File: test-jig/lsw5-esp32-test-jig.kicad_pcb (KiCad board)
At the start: 2 copper layers, 53.8 x 100 mm, 25 parts, among them J1 Conn_02x03_Odd_Even, J2 Conn_02x05_Odd_Even, J3 Conn_02x03_Odd_Even, J4 Conn_02x05_Odd_Even, J5 USB4105-GF-A, SW1 DUT, SW2 USB, U1 LD1117V33, U2 MCP2221AxSL

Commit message: test jig: Fix MCP2221A V_USB capacitor value
DS20005565E-page 17

> The VUSB pin requires an external bypass capacitor
> with a value between 0.22 and 0.47 μF (ceramic cap)
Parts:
- C4: value 1μ -> 470n
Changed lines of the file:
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@@
 			)
 		)
-		(property "Value" "1μ"
+		(property "Value" "470n"
 			(at 0 1.43 90)
 			(layer "F.Fab")

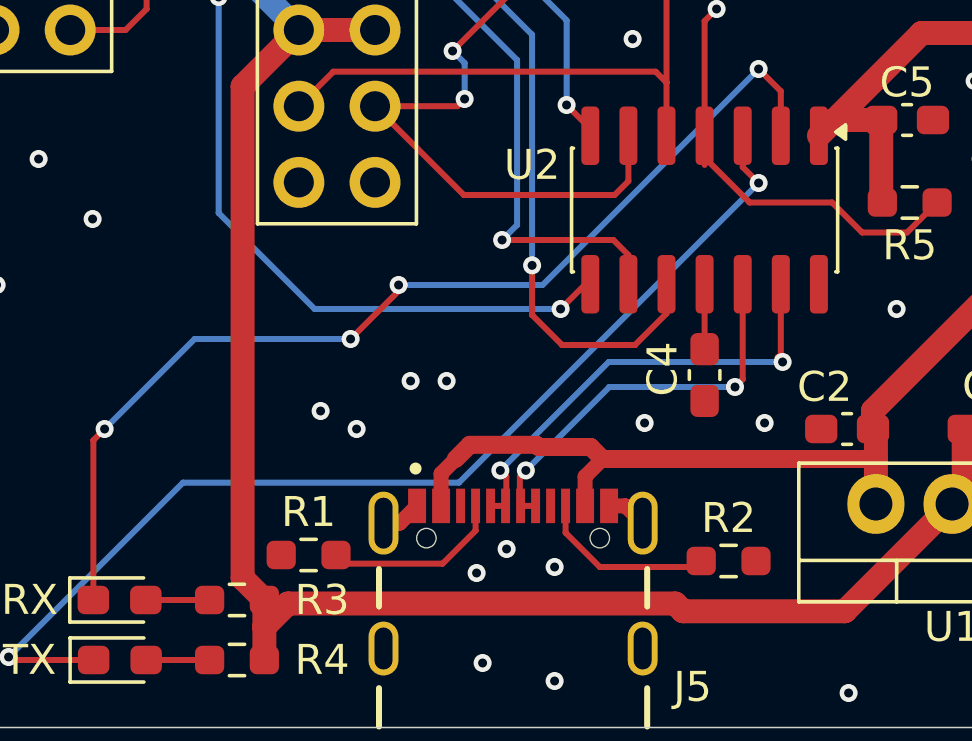
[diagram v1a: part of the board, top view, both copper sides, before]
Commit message: test jig: Fix USB only working on one side
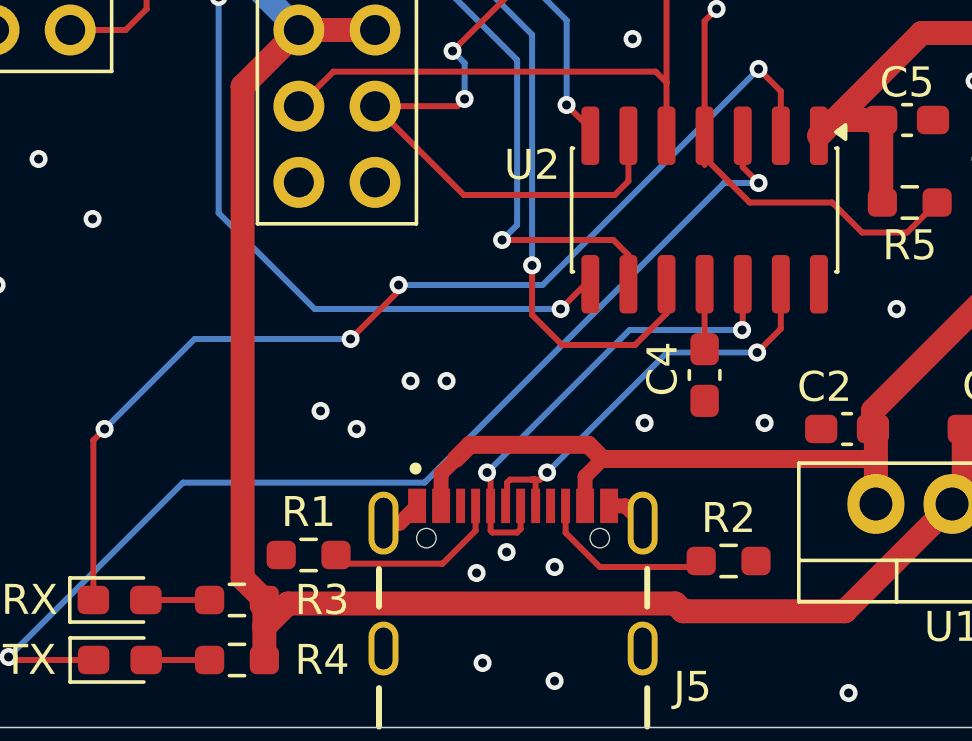
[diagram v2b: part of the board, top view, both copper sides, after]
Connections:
- J5 pad B6: /USB_DN -> /USB_DP
- J5 pad B7: /USB_DP -> /USB_DN
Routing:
- net /USB_DN: track 13.4 -> 15.9 mm
- net /USB_DP: track 15.5 -> 14.6 mm
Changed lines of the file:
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@@
 			(size 0.3 1.15)
 			(layers "F.Cu" "F.Paste")
-			(net 19 "/USB_DN")
+			(net 23 "/USB_DP")
 			(pinfunction "DP2")
 			(pintype "bidirectional")
@@
 			(size 0.3 1.15)
 			(layers "F.Cu" "F.Paste")
-			(net 23 "/USB_DP")
+			(net 19 "/USB_DN")
 			(pinfunction "DN2")
 			(pintype "bidirectional")
@@
 	)
 	(segment
-		(start 148.176865 148.327219)
-		(end 150.394975 148.327219)
-		(width 0.6)
-		(layer "F.Cu")
-		(net 4)
-	)
-	(segment
 		(start 152.016236 149.385848)
 		(end 152.602084 148.8)
@@
 	)
 	(segment
-		(start 147.704084 148.8)
-		(end 148.176865 148.327219)
-		(width 0.6)
-		(layer "F.Cu")
-		(net 4)
-	)
-	(segment
 		(start 152.016236 150.362848)
 		(end 152.016236 149.385848)
@@
 	)
 	(segment
-		(start 152.202084 148.4)
-		(end 152.602084 148.8)
+		(start 148.176865 148.327219)
+		(end 152.129303 148.327219)
 		(width 0.6)
 		(layer "F.Cu")
@@
 	)
 	(segment
+		(start 147.704084 148.8)
+		(end 148.176865 148.327219)
+		(width 0.6)
+		(layer "F.Cu")
+		(net 4)
+	)
+	(segment
 		(start 161.8875 137.5)
 		(end 160.335 137.5)
@@
 	)
 	(segment
-		(start 150.467756 148.4)
-		(end 152.202084 148.4)
-		(width 0.6)
+		(start 160.335 137.5)
+		(end 159.81 138.025)
+		(width 0.8)
 		(layer "F.Cu")
 		(net 4)
 	)
 	(segment
-		(start 150.394975 148.327219)
-		(end 150.467756 148.4)
+		(start 152.129303 148.327219)
+		(end 152.602084 148.8)
 		(width 0.6)
 		(layer "F.Cu")
@@
 	)
 	(segment
-		(start 160.335 137.5)
-		(end 159.81 138.025)
-		(width 0.8)
-		(layer "F.Cu")
-		(net 4)
-	)
-	(segment
 		(start 156 145.1375)
 		(end 156 142.975)
@@
 	)
 	(via
-		(at 149.4 151.8)
+		(at 149.4 151.904)
 		(size 0.6)
 		(drill 0.3)
@@
 	)
 	(segment
-		(start 157.8 139.6)
-		(end 147.813152 149.586848)
+		(start 146.663152 149.586848)
+		(end 138.613152 149.586848)
 		(width 0.2)
 		(layer "B.Cu")
@@
 	)
 	(segment
-		(start 147.813152 149.586848)
-		(end 138.613152 149.586848)
+		(start 156.65 139.6)
+		(end 146.663152 149.586848)
+		(width 0.2)
+		(layer "B.Cu")
+		(net 13)
+	)
+	(segment
+		(start 157.8 139.6)
+		(end 156.65 139.6)
 		(width 0.2)
 		(layer "B.Cu")
@@
 	)
 	(segment
-		(start 149.866236 150.362848)
-		(end 150.366236 150.362848)
+		(start 149.866236 151.133764)
+		(end 149.866236 150.362848)
+		(width 0.2)
+		(layer "F.Cu")
+		(net 19)
+	)
+	(segment
+		(start 148.866236 149.366236)
+		(end 148.75 149.25)
 		(width 0.2)
 		(layer "F.Cu")
@@
 	)
 	(segment
-		(start 149.841237 149.381218)
-		(end 150.041236 149.181219)
+		(start 157.27 142.975)
+		(end 157.27 144.48)
 		(width 0.2)
 		(layer "F.Cu")
@@
 	)
 	(segment
-		(start 157.01334 146.4)
-		(end 157.27 146.14334)
+		(start 157.27 144.48)
+		(end 157.25 144.5)
+		(width 0.2)
+		(layer "F.Cu")
+		(net 19)
+	)
+	(segment
+		(start 148.866236 150.362848)
+		(end 148.866236 149.366236)
 		(width 0.2)
 		(layer "F.Cu")
@@
 	)
 	(segment
-		(start 149.841237 150.337849)
-		(end 149.841237 149.381218)
+		(start 149.75 151.25)
+		(end 149.866236 151.133764)
+		(width 0.2)
+		(layer "F.Cu")
+		(net 19)
+	)
+	(segment
+		(start 148.866236 150.362848)
+		(end 148.866236 151.189848)
+		(width 0.2)
+		(layer "F.Cu")
+		(net 19)
+	)
+	(segment
+		(start 148.866236 151.189848)
+		(end 148.926388 151.25)
 		(width 0.2)
 		(layer "F.Cu")
@@
 	)
 	(segment
-		(start 157.27 146.14334)
-		(end 157.27 142.975)
+		(start 148.926388 151.25)
+		(end 149.75 151.25)
 		(width 0.2)
 		(layer "F.Cu")
@@
 	)
 	(via
-		(at 157.01334 146.4)
+		(at 148.75 149.25)
 		(size 0.6)
 		(drill 0.3)
@@
 	)
 	(via
-		(at 150.041236 149.181219)
+		(at 157.25 144.5)
 		(size 0.6)
 		(drill 0.3)
@@
 	)
 	(segment
-		(start 152.822455 146.4)
-		(end 157.01334 146.4)
+		(start 148.75 149.25)
+		(end 153.5 144.5)
 		(width 0.2)
 		(layer "B.Cu")
@@
 	)
 	(segment
-		(start 150.041236 149.181219)
-		(end 152.822455 146.4)
+		(start 153.5 144.5)
+		(end 157.25 144.5)
 		(width 0.2)
 		(layer "B.Cu")
@@
 	)
 	(segment
-		(start 158.54 145.506172)
-		(end 158.54 142.975)
+		(start 150.513152 149.486848)
+		(end 150.75 149.25)
 		(width 0.2)
 		(layer "F.Cu")
@@
 	)
 	(segment
-		(start 149.391235 149.381218)
-		(end 149.191236 149.181219)
+		(start 157.75 145.25)
+		(end 158.54 144.46)
 		(width 0.2)
 		(layer "F.Cu")
@@
 	)
 	(segment
-		(start 158.433828 145.4)
-		(end 158.6 145.566172)
+		(start 149.415236 149.870612)
+		(end 149.415236 149.584764)
 		(width 0.2)
 		(layer "F.Cu")
@@
 	)
 	(segment
-		(start 158.6 145.566172)
-		(end 158.54 145.506172)
+		(start 149.513152 149.486848)
+		(end 150.236848 149.486848)
 		(width 0.2)
 		(layer "F.Cu")
@@
 	)
 	(segment
-		(start 149.391235 150.337849)
-		(end 149.391235 149.381218)
+		(start 149.415236 149.584764)
+		(end 149.513152 149.486848)
 		(width 0.2)
 		(layer "F.Cu")
@@
 	)
 	(segment
-		(start 148.866236 150.362848)
-		(end 149.366236 150.362848)
+		(start 150.236848 149.486848)
+		(end 150.513152 149.486848)
+		(width 0.2)
+		(layer "F.Cu")
+		(net 23)
+	)
+	(segment
+		(start 150.353084 149.486848)
+		(end 150.366236 149.5)
+		(width 0.2)
+		(layer "F.Cu")
+		(net 23)
+	)
+	(segment
+		(start 150.236848 149.486848)
+		(end 150.353084 149.486848)
+		(width 0.2)
+		(layer "F.Cu")
+		(net 23)
+	)
+	(segment
+		(start 150.366236 150.362848)
+		(end 150.366236 149.5)
+		(width 0.2)
+		(layer "F.Cu")
+		(net 23)
+	)
+	(segment
+		(start 149.366236 150.362848)
+		(end 149.366236 149.919612)
+		(width 0.2)
+		(layer "F.Cu")
+		(net 23)
+	)
+	(segment
+		(start 158.54 144.46)
+		(end 158.54 142.975)
+		(width 0.2)
+		(layer "F.Cu")
+		(net 23)
+	)
+	(segment
+		(start 149.366236 149.919612)
+		(end 149.415236 149.870612)
 		(width 0.2)
 		(layer "F.Cu")
@@
 	)
 	(via
-		(at 158.6 145.566172)
+		(at 150.75 149.25)
 		(size 0.6)
 		(drill 0.3)
@@
 	)
 	(via
-		(at 149.191236 149.181219)
+		(at 157.75 145.25)
 		(size 0.6)
 		(drill 0.3)
@@
 	)
 	(segment
-		(start 152.806283 145.566172)
-		(end 158.6 145.566172)
+		(start 150.75 149.25)
+		(end 154.75 145.25)
 		(width 0.2)
 		(layer "B.Cu")
@@
 	)
 	(segment
-		(start 149.191236 149.181219)
-		(end 152.806283 145.566172)
+		(start 154.75 145.25)
+		(end 157.75 145.25)
 		(width 0.2)
 		(layer "B.Cu")
